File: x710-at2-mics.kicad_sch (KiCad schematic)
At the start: 59 parts, among them U4 EZX710AT2_S_LMR5, U5 74LVC1G07_SOT-753

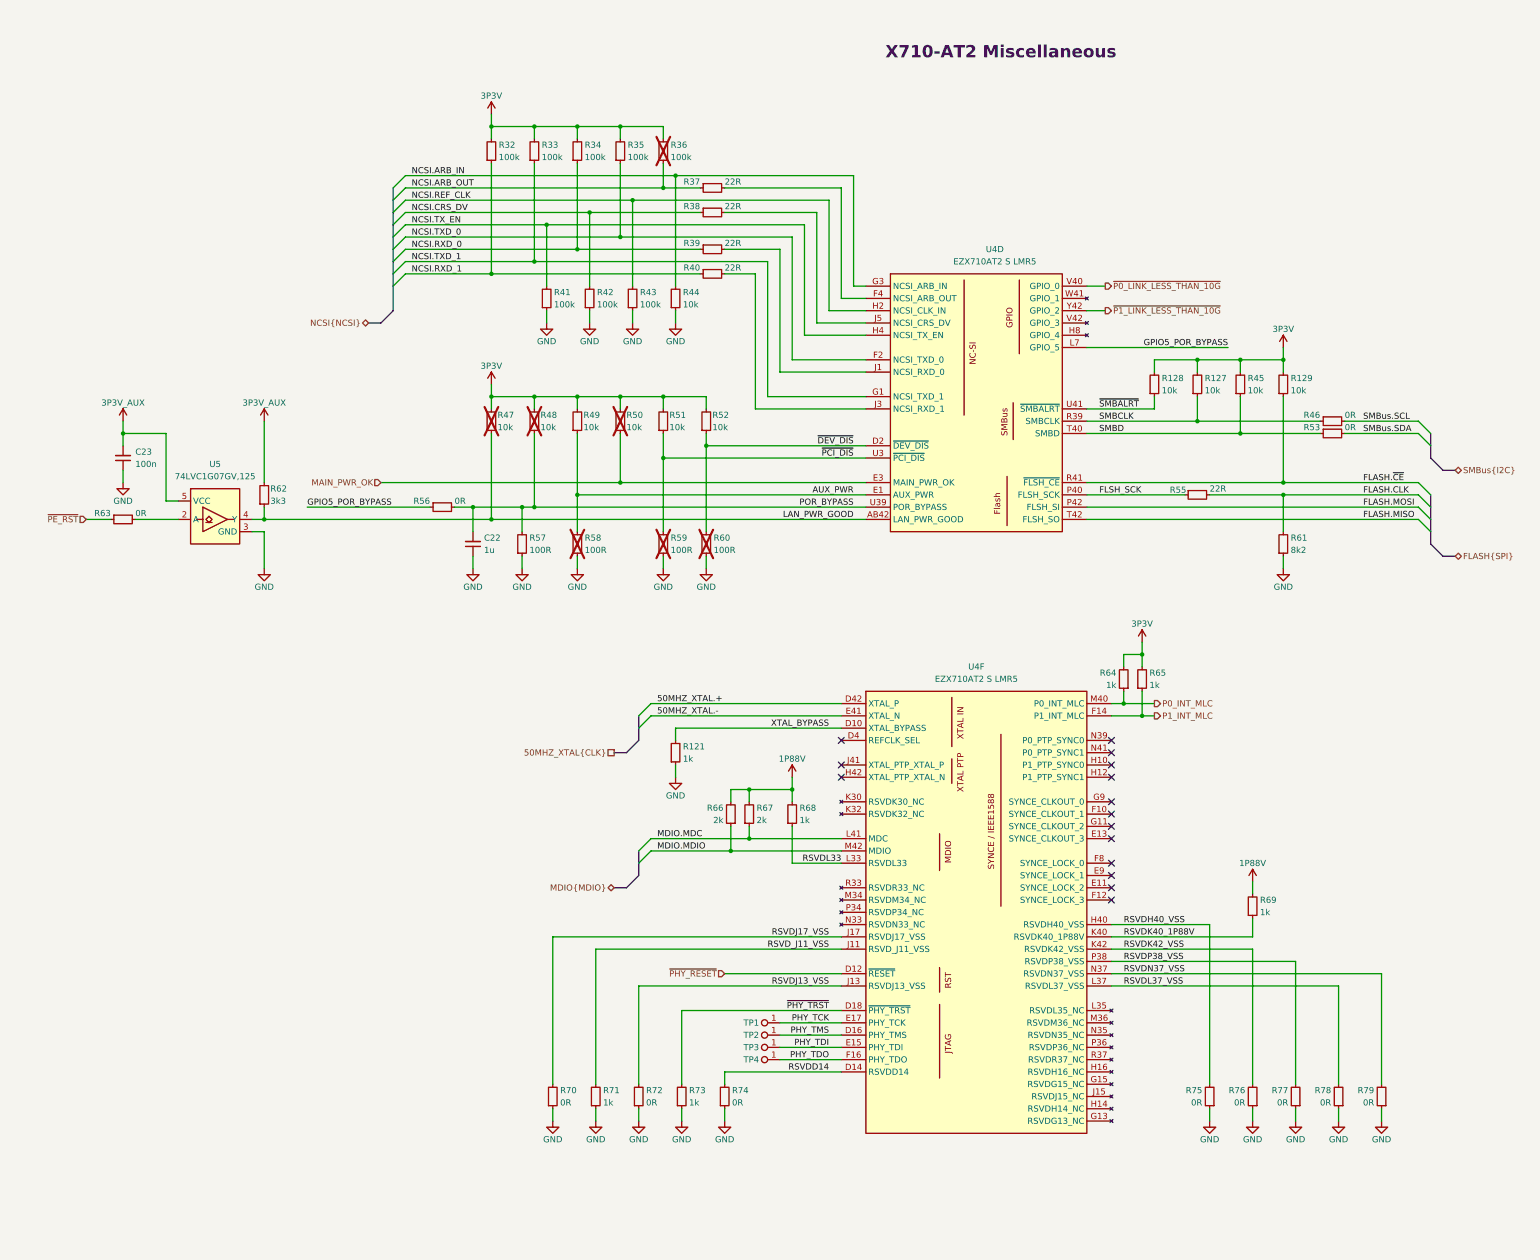
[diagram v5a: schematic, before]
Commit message: [#80813] Change 3V3 and 1V88 power rails names
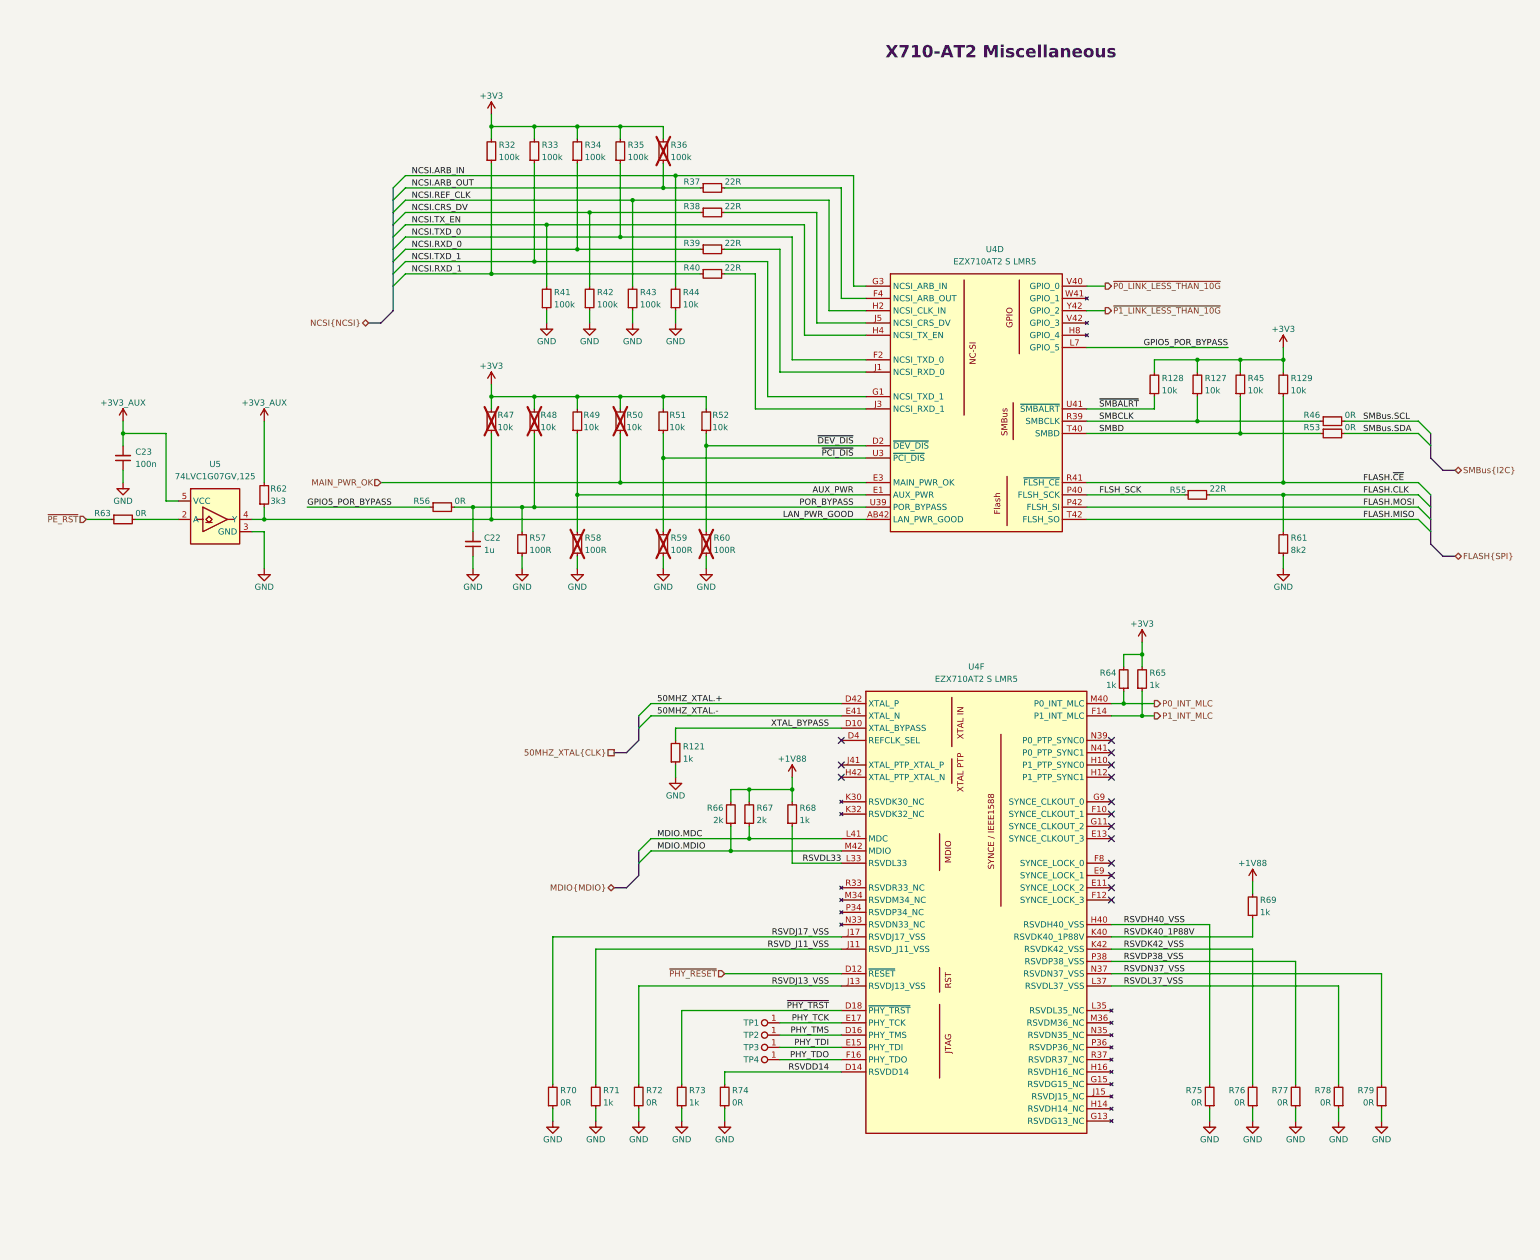
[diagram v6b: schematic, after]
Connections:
- net 1P88V renamed +1V88
- net 3P3V renamed +3V3
- net 3P3V_AUX renamed +3V3_AUX

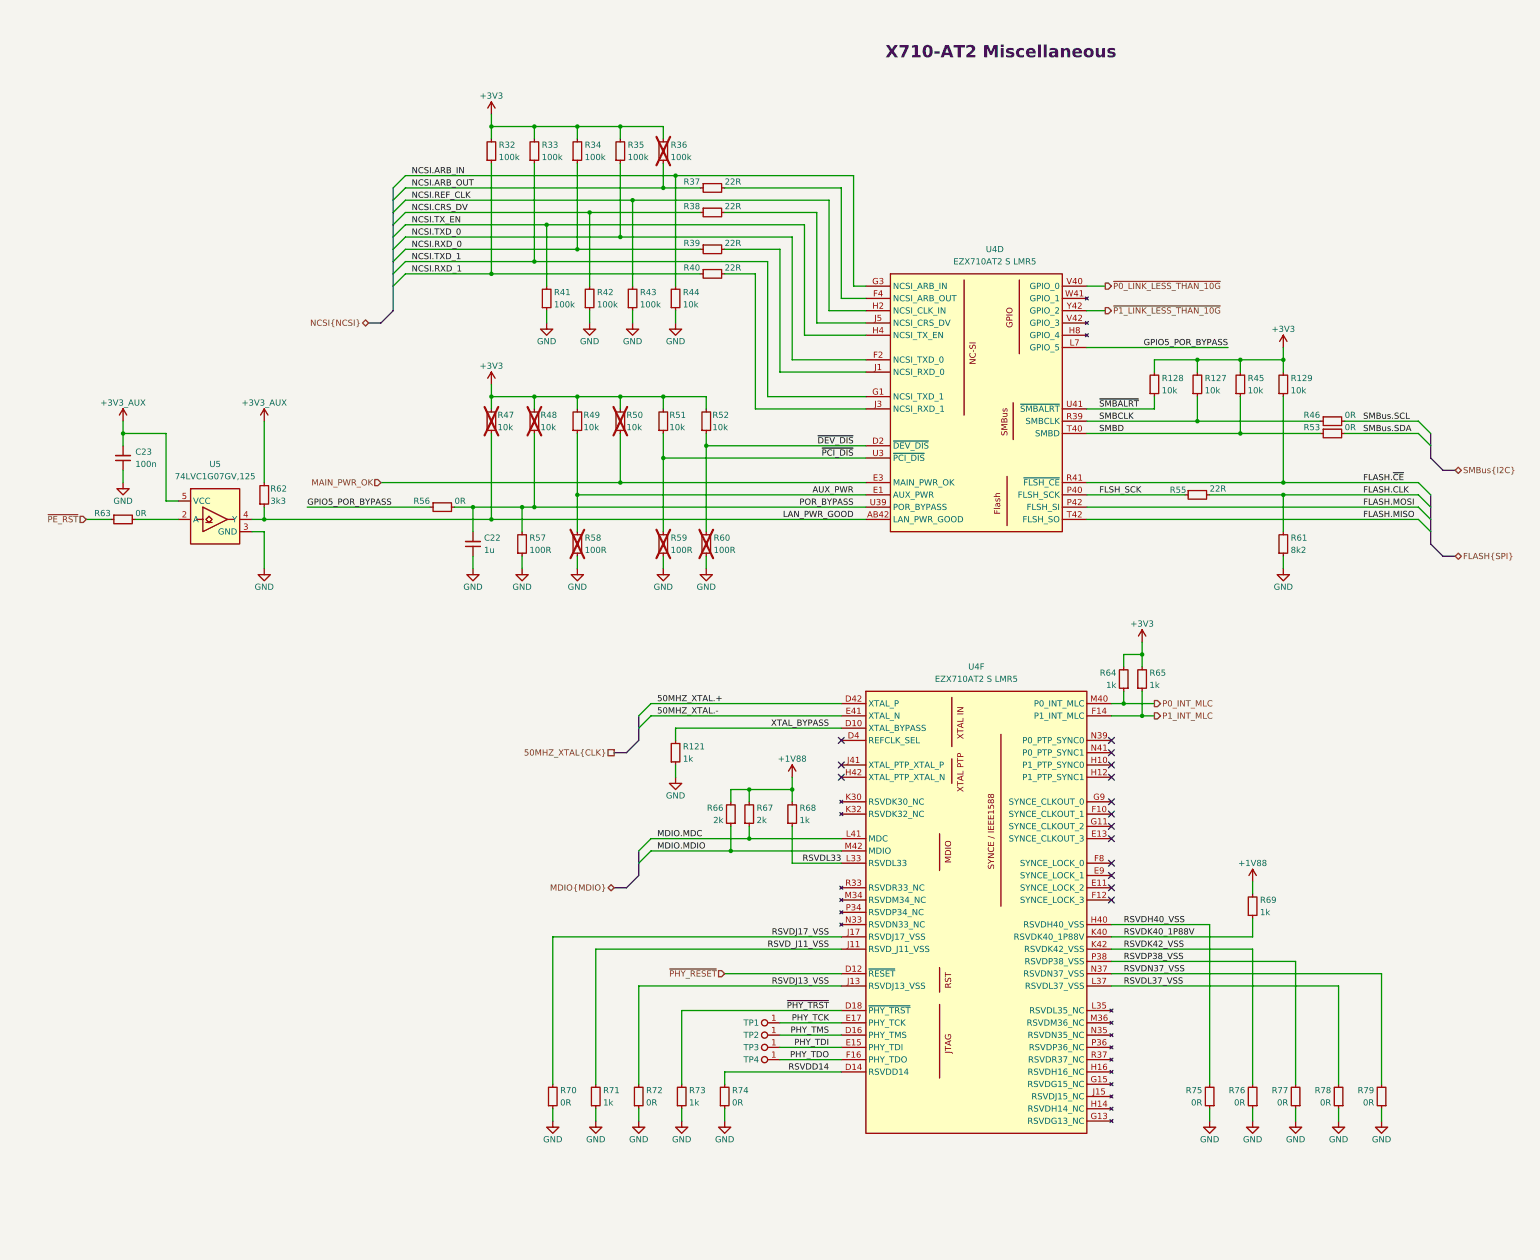
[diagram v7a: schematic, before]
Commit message: [#80813] Add OCuLink connector
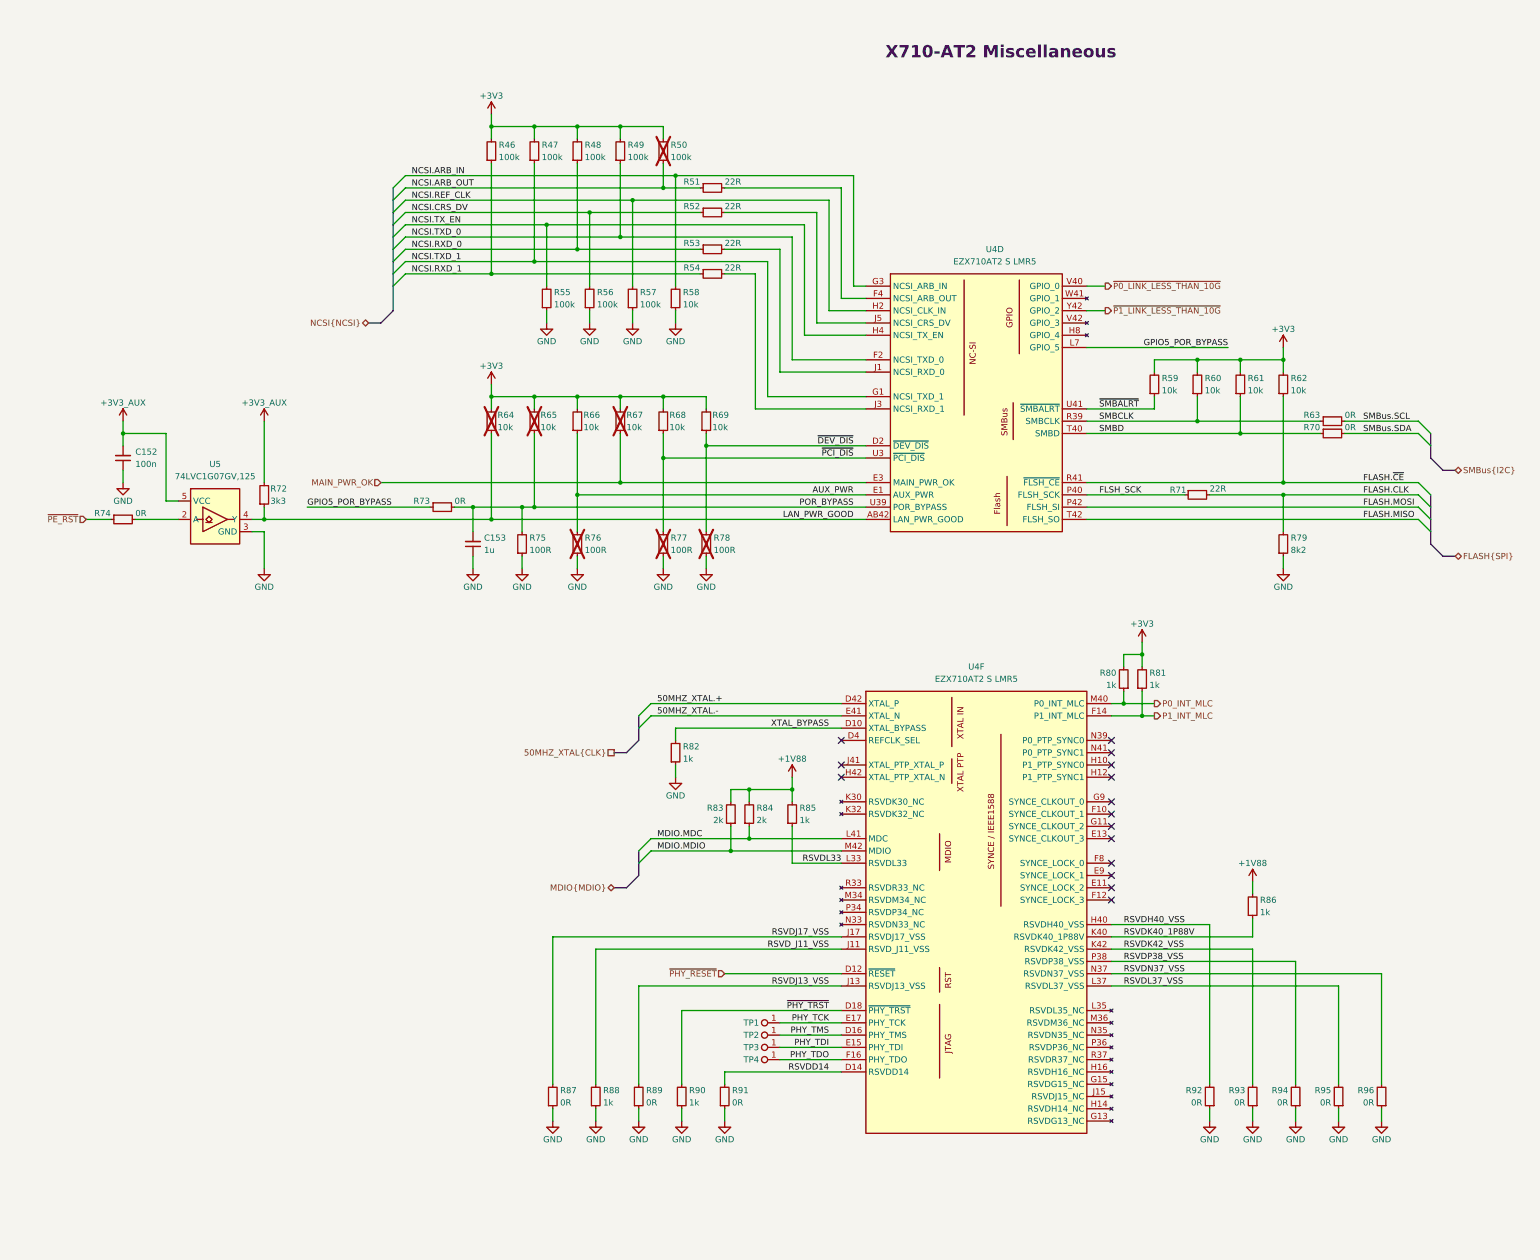
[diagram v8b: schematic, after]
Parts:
- renumbered C23 to C152, C22 to C153, R32 to R46, R33 to R47, R34 to R48, R35 to R49, R36 to R50, R37 to R51, R38 to R52, R39 to R53, R40 to R54, R41 to R55, R42 to R56, R43 to R57, R44 to R58, R128 to R59, R127 to R60, R45 to R61, R129 to R62, R46 to R63, R47 to R64, R48 to R65, R49 to R66, R50 to R67, R51 to R68, R52 to R69, R53 to R70, R55 to R71, R62 to R72, R56 to R73, R63 to R74, R57 to R75, R58 to R76, R59 to R77, R60 to R78, R61 to R79, R64 to R80, R65 to R81, R121 to R82, R66 to R83, R67 to R84, R68 to R85, R69 to R86, R70 to R87, R71 to R88, R72 to R89, R73 to R90, R74 to R91, R75 to R92, R76 to R93, R77 to R94, R78 to R95, R79 to R96
